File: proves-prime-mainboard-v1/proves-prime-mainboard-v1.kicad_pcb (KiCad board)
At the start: 2 copper layers, 100 parts, among them IC4 LT3652IMSE#PBF, J1 Breakout, J10 Conn_Coaxial, J9 Conn_Coaxial, U10 RFM9xBreakout, U11 MCP9808T-E/MS, U12 INA219AxD, U13 INA219AxD, U2 TLV1704, U5 LSM6DSOTR, U6 LSM303AGRTR

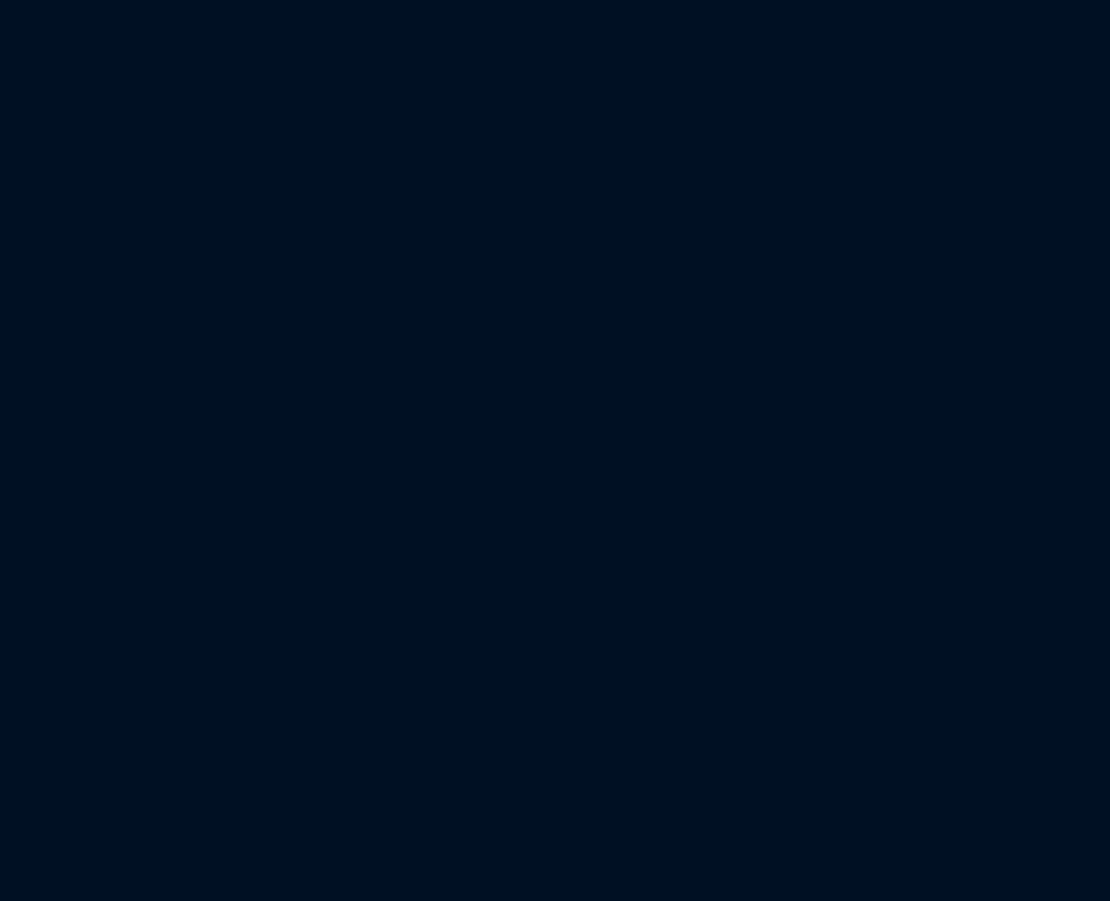
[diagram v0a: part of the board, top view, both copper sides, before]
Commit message: Added Burnwire Candidates
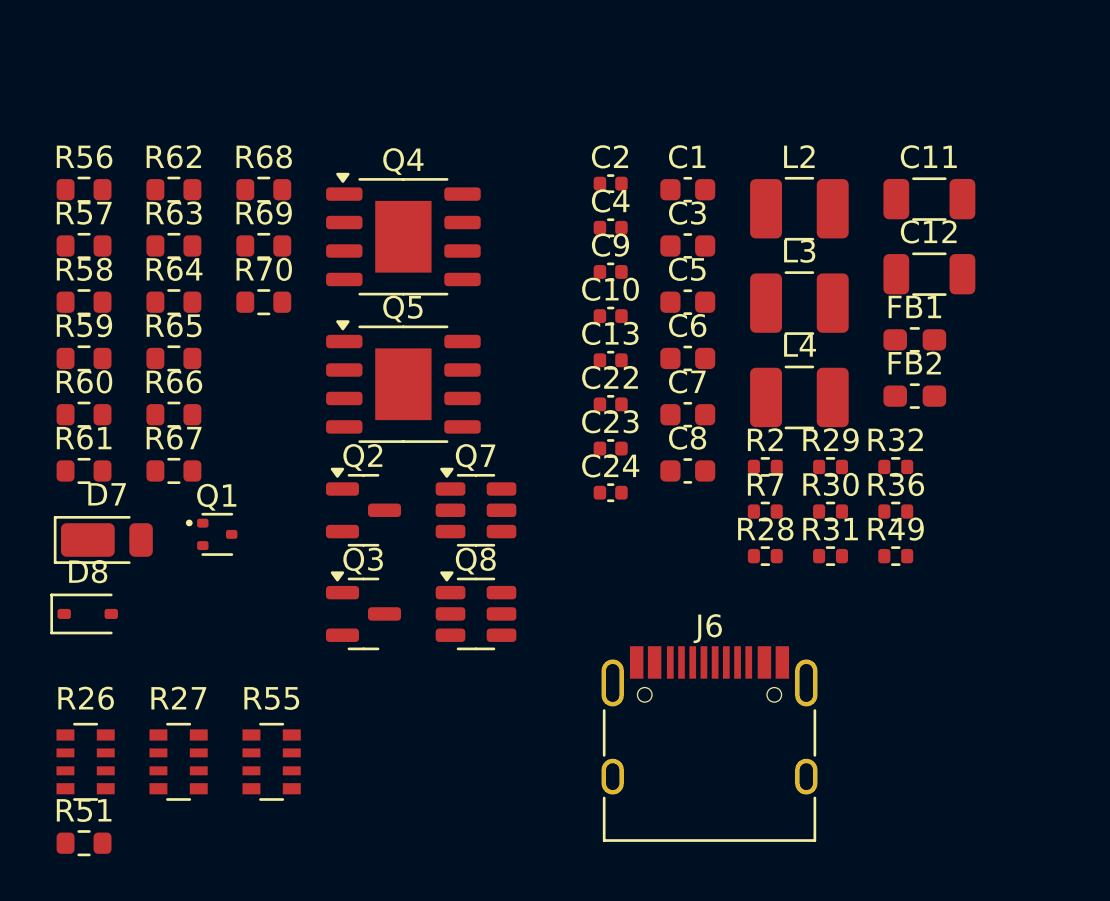
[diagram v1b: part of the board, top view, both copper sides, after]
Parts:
- added C1: 4.7uF, Capacitor_SMD:C_0603_1608Metric, F.Cu at (120.6, 119.2)
- added C10: 0.1uF, Capacitor_SMD:C_0402_1005Metric, F.Cu at (117.2, 124.8)
- added C11: 47uF, Capacitor_SMD:C_1206_3216Metric, F.Cu at (131.4, 119.6)
- added C12: 68uF, Capacitor_SMD:C_1206_3216Metric, F.Cu at (131.4, 123.0)
- added C13: 10pF, Capacitor_SMD:C_0402_1005Metric, F.Cu at (117.2, 126.8)
- added C2: 10nF, Capacitor_SMD:C_0402_1005Metric, F.Cu at (117.2, 118.9)
- added C22: 4.7pF, Capacitor_SMD:C_0402_1005Metric, F.Cu at (117.2, 128.8)
- added C23: 1uF, Capacitor_SMD:C_0402_1005Metric, F.Cu at (117.2, 130.8)
- added C24: 1uF, Capacitor_SMD:C_0402_1005Metric, F.Cu at (117.2, 132.7)
- added C3: 4.7uF, Capacitor_SMD:C_0603_1608Metric, F.Cu at (120.6, 121.7)
- added C4: 10nF, Capacitor_SMD:C_0402_1005Metric, F.Cu at (117.2, 120.9)
- added C5: 4.7uF, Capacitor_SMD:C_0603_1608Metric, F.Cu at (120.6, 124.2)
- added C6: 4.7uF, Capacitor_SMD:C_0603_1608Metric, F.Cu at (120.6, 126.7)
- added C7: 4.7uF, Capacitor_SMD:C_0603_1608Metric, F.Cu at (120.6, 129.2)
- added C8: 4.7uF, Capacitor_SMD:C_0603_1608Metric, F.Cu at (120.6, 131.8)
- added C9: 0.1uF, Capacitor_SMD:C_0402_1005Metric, F.Cu at (117.2, 122.9)
- added D7: DFLS130L, Diode_SMD:D_PowerDI-123, F.Cu at (94.7, 134.8)
- added D8: 1N4151WS, Diode_SMD:D_SOD-323, F.Cu at (93.8, 138.1)
- added FB1: FerriteBead, Inductor_SMD:L_0603_1608Metric_Pad1.05x0.95mm_HandSolder, F.Cu at (130.7, 125.9)
- added FB2: FerriteBead, Inductor_SMD:L_0603_1608Metric_Pad1.05x0.95mm_HandSolder, F.Cu at (130.7, 128.4)
- added J6: USB_C_Receptacle_USB2.0_16P, Connector_USB:USB_C_Receptacle_HRO_TYPE-C-31-M-12, F.Cu at (121.6, 144.3)
- added L2: 4.7uH, Inductor_SMD:L_1210_3225Metric_Pad1.42x2.65mm_HandSolder, F.Cu at (125.6, 120.1)
- added L3: 4.7uH, Inductor_SMD:L_1210_3225Metric_Pad1.42x2.65mm_HandSolder, F.Cu at (125.6, 124.3)
- added L4: 4.7uH, Inductor_SMD:L_1210_3225Metric_Pad1.42x2.65mm_HandSolder, F.Cu at (125.6, 128.5)
- added Q1: MMBT2222AT, Package_TO_SOT_SMD:SOT-523, F.Cu at (99.6, 134.6)
- added Q2: IRLML2803, Package_TO_SOT_SMD:SOT-23, F.Cu at (106.1, 133.5)
- added Q3: IRLML2803, Package_TO_SOT_SMD:SOT-23, F.Cu at (106.1, 138.1)
- added Q4: NDS8434, Package_SO:SOIC-8-1EP_3.9x4.9mm_P1.27mm_EP2.514x3.2mm, F.Cu at (107.9, 121.3)
- added Q5: NDS8434, Package_SO:SOIC-8-1EP_3.9x4.9mm_P1.27mm_EP2.514x3.2mm, F.Cu at (107.9, 127.9)
- added Q7: DMP2240UDM-7, Package_TO_SOT_SMD:SOT-23-6, F.Cu at (111.2, 133.5)
- added Q8: DMP2240UDM-7, Package_TO_SOT_SMD:SOT-23-6, F.Cu at (111.2, 138.1)
- added R2: 60.4k, Resistor_SMD:R_0402_1005Metric, F.Cu at (124.1, 131.6)
- added R26: 10k, Resistor_SMD:R_Array_Convex_4x0603, F.Cu at (93.7, 144.7)
- added R27: 10k, Resistor_SMD:R_Array_Convex_4x0603, F.Cu at (97.9, 144.7)
- added R28: 0, Resistor_SMD:R_0402_1005Metric, F.Cu at (124.1, 135.6)
- added R29: 0, Resistor_SMD:R_0402_1005Metric, F.Cu at (127.0, 131.6)
- added R30: 1k, Resistor_SMD:R_0402_1005Metric, F.Cu at (127.0, 133.6)
- added R31: 1k, Resistor_SMD:R_0402_1005Metric, F.Cu at (127.0, 135.6)
- added R32: 1M, Resistor_SMD:R_0402_1005Metric, F.Cu at (129.9, 131.6)
- added R36: 1M, Resistor_SMD:R_0402_1005Metric, F.Cu at (129.9, 133.6)
- added R49: 243k, Resistor_SMD:R_0402_1005Metric, F.Cu at (129.9, 135.6)
- added R51: 10K, Resistor_SMD:R_0603_1608Metric, F.Cu at (93.7, 148.4)
- added R55: 10k, Resistor_SMD:R_Array_Convex_4x0603, F.Cu at (102.0, 144.7)
- added R56: 10k, Resistor_SMD:R_0603_1608Metric, F.Cu at (93.7, 119.2)
- added R57: 100, Resistor_SMD:R_0603_1608Metric, F.Cu at (93.7, 121.7)
- added R58: 634k, Resistor_SMD:R_0603_1608Metric, F.Cu at (93.7, 124.2)
- added R59: 10k, Resistor_SMD:R_0603_1608Metric, F.Cu at (93.7, 126.7)
- added R60: 10k, Resistor_SMD:R_0603_1608Metric, F.Cu at (93.7, 129.2)
- added R61: 4.7k, Resistor_SMD:R_0603_1608Metric, F.Cu at (93.7, 131.8)
- added R62: 4.7k, Resistor_SMD:R_0603_1608Metric, F.Cu at (97.7, 119.2)
- added R63: 100k, Resistor_SMD:R_0603_1608Metric, F.Cu at (97.7, 121.7)
- added R64: 100k, Resistor_SMD:R_0603_1608Metric, F.Cu at (97.7, 124.2)
- added R65: 10k, Resistor_SMD:R_0603_1608Metric, F.Cu at (97.7, 126.7)
- added R66: 10k, Resistor_SMD:R_0603_1608Metric, F.Cu at (97.7, 129.2)
- added R67: 10k, Resistor_SMD:R_0603_1608Metric, F.Cu at (97.7, 131.8)
- added R68: 1k, Resistor_SMD:R_0603_1608Metric, F.Cu at (101.7, 119.2)
- added R69: 47k, Resistor_SMD:R_0603_1608Metric, F.Cu at (101.7, 121.7)
- added R7: 110k, Resistor_SMD:R_0402_1005Metric, F.Cu at (124.1, 133.6)
- added R70: 10k, Resistor_SMD:R_0603_1608Metric, F.Cu at (101.7, 124.2)
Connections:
- net GND renamed BURN
- A1 pad 10: unconnected-(A1-GPIO10-Pad10) -> RF1_RST
- A1 pad 11: unconnected-(A1-GPIO11-Pad11) -> RF1_IO4
- A1 pad 12: unconnected-(A1-GPIO12-Pad12) -> RF1_IO0
- A1 pad 13: unconnected-(A1-GPIO13-Pad13) -> RF2_RST
- A1 pad 14: unconnected-(A1-GPIO14-Pad14) -> RF2_IO4
- A1 pad 15: unconnected-(A1-GPIO15-Pad15) -> RF2_IO0
- A1 pad 18: unconnected-(A1-GPIO18-Pad18) -> ENABLE_3V3
- A1 pad 19: unconnected-(A1-GPIO19-Pad19) -> ENABLE_5V
- A1 pad 20: unconnected-(A1-GPIO20-Pad20) -> ~{CHARGE}
- A1 pad 24: unconnected-(A1-GPIO24-Pad24) -> WDT_WDI
- A1 pad 47: unconnected-(A1-GPIO47_ADC7-Pad47) -> NEOPIX
- A1 pad 49: unconnected-(A1-SWDIO-Pad49) -> SWDIO
- A1 pad 50: unconnected-(A1-USB_DM-Pad50) -> Net-(A1-USB_DM)
- A1 pad 51: unconnected-(A1-SWCLK-Pad51) -> SWCLK
- A1 pad 52: unconnected-(A1-USB_DP-Pad52) -> Net-(A1-USB_DP)
- A1 pad 57: unconnected-(A1-VBUS-Pad57) -> V_USB
- A1 pad 8: unconnected-(A1-GPIO8-Pad8) -> ~{MUX_RESET}
- A1 pad 9: unconnected-(A1-GPIO9-Pad9) -> RTC_INT
- D1 pad 2: RX -> UART0_RX
- D2 pad 2: TX -> UART0_TX
- IC4 pad 4: CHRG' -> ~{CHARGE}
- R39 pad 2: SPI0_CS0 -> Net-(U10-CS)
- R43 pad 2: CHRG' -> ~{CHARGE}
- U10 pad 5: SPI0_CS0 -> Net-(U10-CS)
- U11 pad 1: unconnected-(U11-SDA-Pad1) -> I2C0_SDA
- U11 pad 2: unconnected-(U11-SCL-Pad2) -> I2C0_SCL
- U5 pad 13: SCL1 -> I2C0_SCL
- U5 pad 14: SDA1 -> I2C0_SDA
- U6 pad 1: SCL1 -> I2C0_SCL
- U6 pad 4: SDA1 -> I2C0_SDA
